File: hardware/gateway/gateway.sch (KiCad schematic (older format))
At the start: 27 parts, among them J1 FTDI, J2 Conn_Coaxial, J3 Raspberry_Pi_2_3, U1 RFM69HW, U2 DS1307Z+, U3 AP130-xxY, Y1 32768

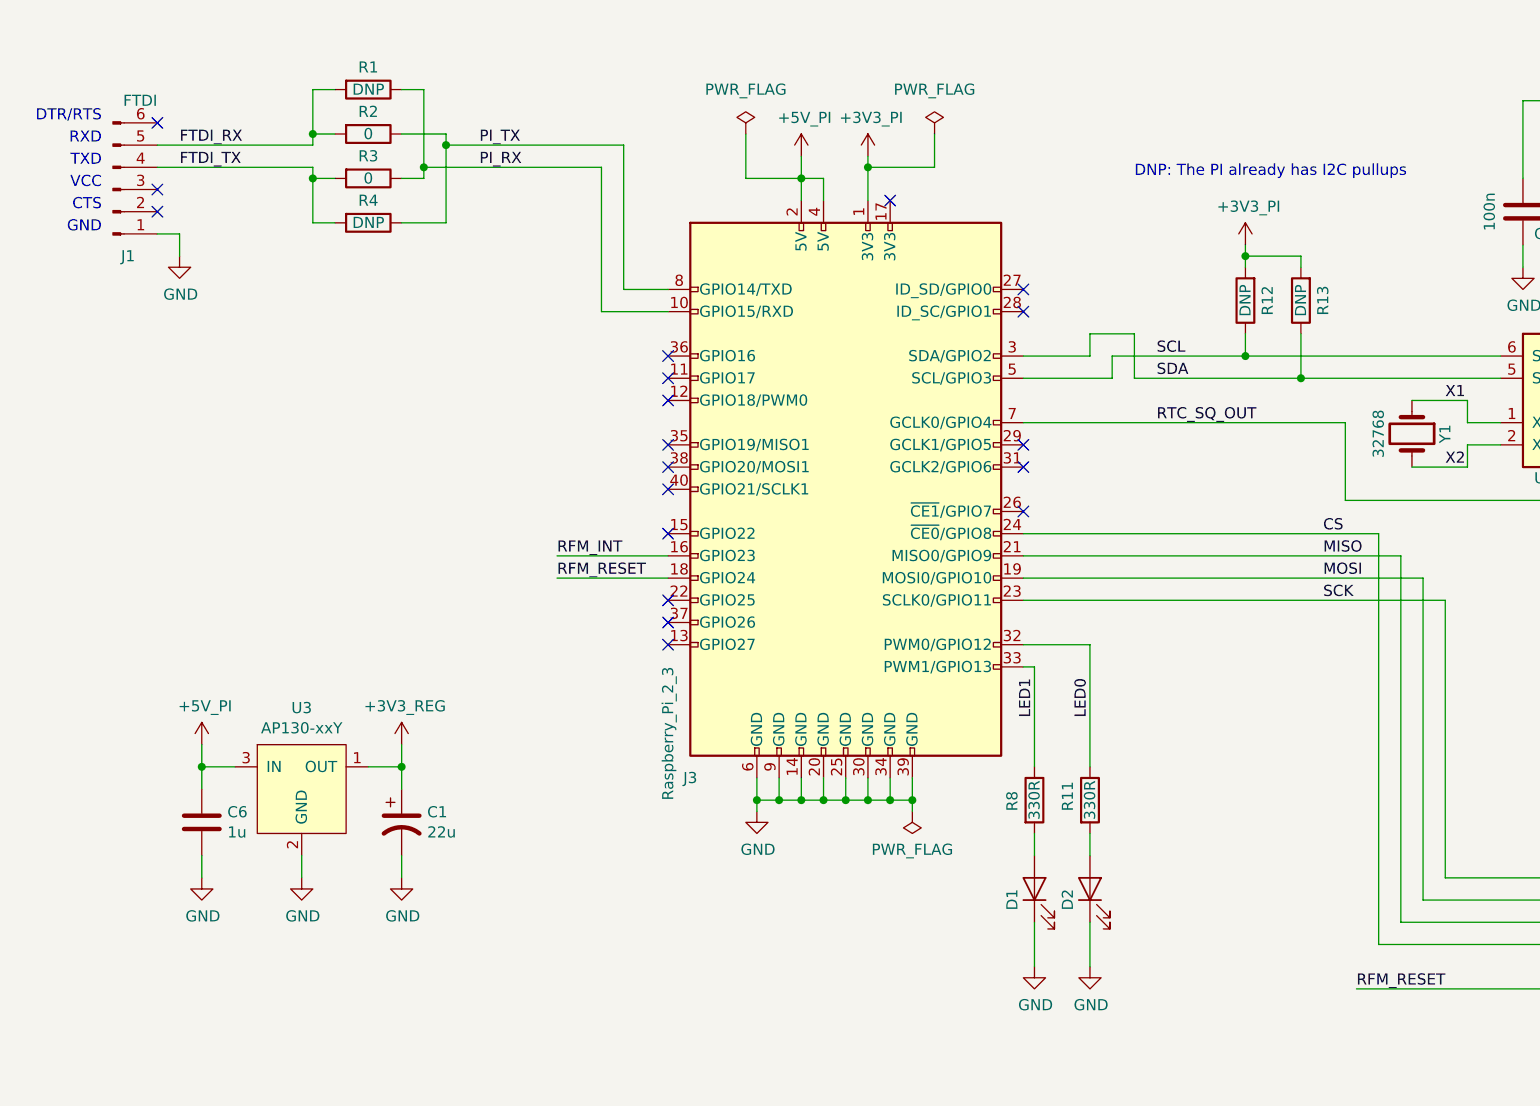
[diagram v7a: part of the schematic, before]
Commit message: Added extra input cap and CS pullup to gateway
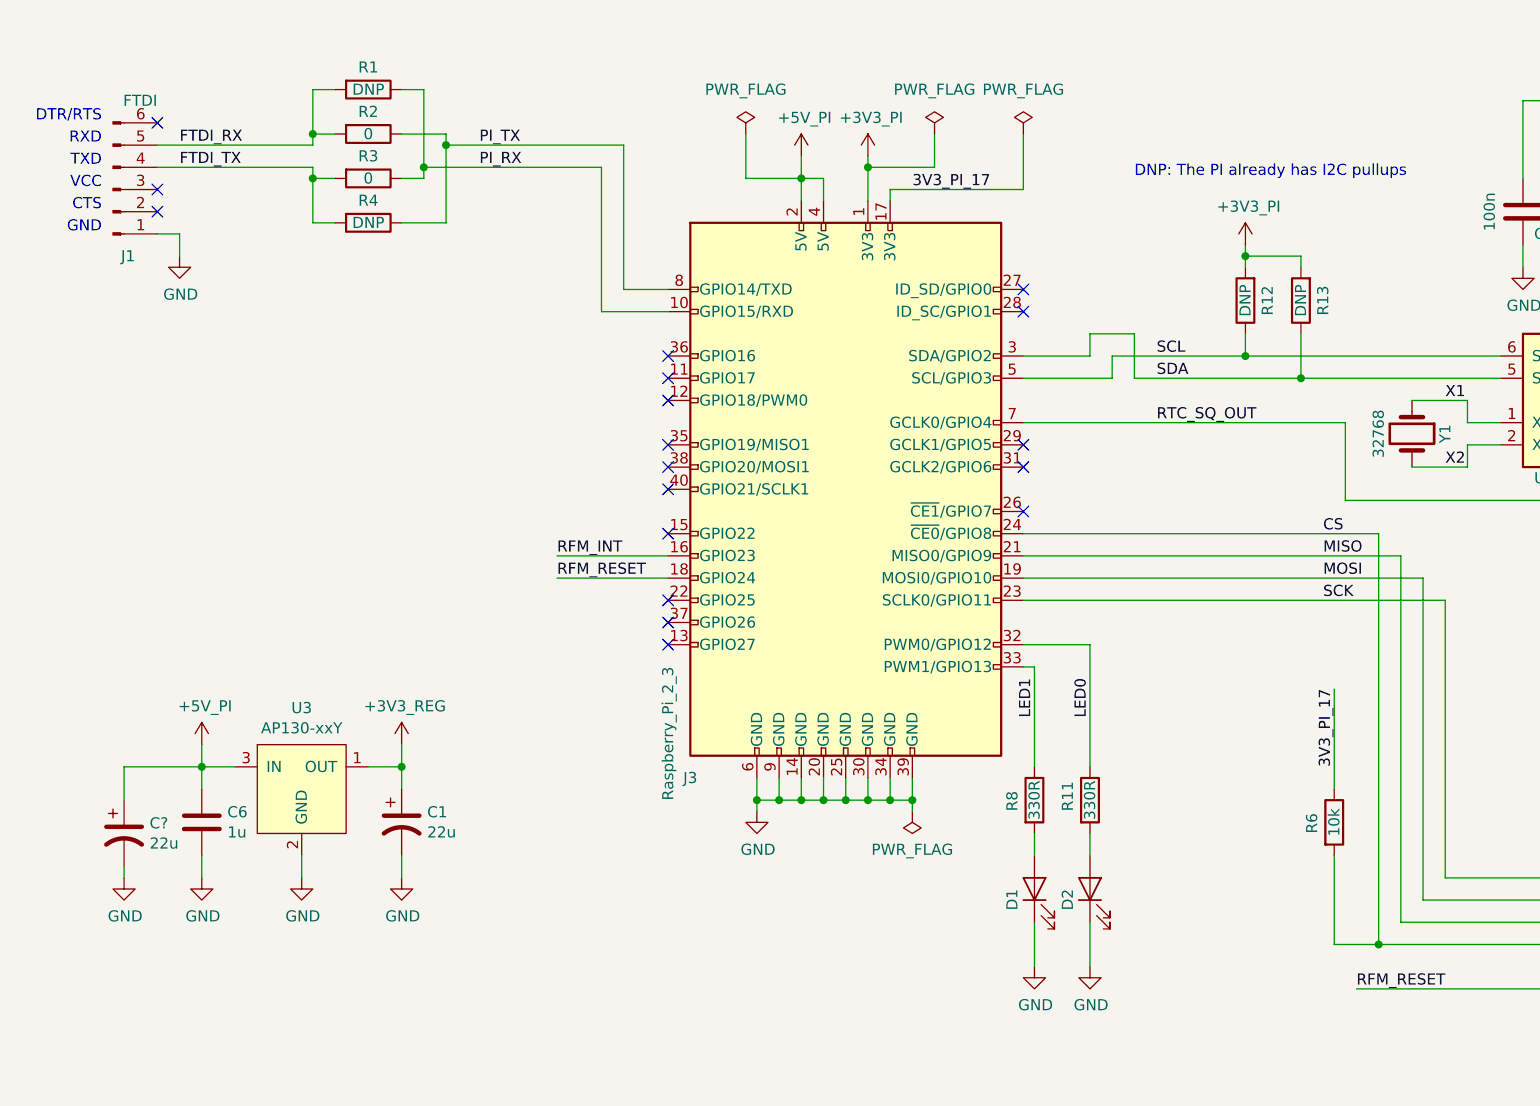
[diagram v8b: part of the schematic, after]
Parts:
- added C?: 22u, Capacitor_SMD:CP_Elec_5x5.3, symbol Device:CP1
- added R6: 10k, Resistor_SMD:R_0603_1608Metric_Pad1.05x0.95mm_HandSolder, symbol Device:R
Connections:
- net +5V_PI: now also C?.1
- net CS: now also R6.2
- net GND: now also C?.2
- net 3V3_PI_17: now reaches J3.17 (3V3)
- net 3V3_PI_17: now also R6.1
- no-connect marks 24 -> 23
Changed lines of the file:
@@
 Wire Wire Line
 	4200 1250 4200 1350
-NoConn ~ 4600 1350
 $Comp
 L humidity:+5V_PI #PWR0104
@@
 Wire Wire Line
 	3950 1250 4200 1250
+$Comp
+L Device:R R6
+U 1 1 5D2FBF60
+P 6600 4150
+F 0 "R6" V 6500 4100 50  0000 L CNN
+F 1 "10k" V 6600 4150 50  0000 C CNN
+F 2 "Resistor_SMD:R_0603_1608Metric_Pad1.05x0.95mm_HandSolder" V 6530 4150 50  0001 C CNN
+F 3 "~" H 6600 4150 50  0001 C CNN
+F 4 "https://www.tme.eu/se/en/details/crcw060310k0fktabc/0603-smd-resistors/vishay/" H -350 2350 50  0001 C CNN "TME Link"
+F 5 "0.12458" H -350 2350 50  0001 C CNN "TME Price"
+	1    6600 4150
+	1    0    0    -1
+$EndComp
+Wire Wire Line
+	6600 4300 6600 4700
+Wire Wire Line
+	6600 4700 6800 4700
+Connection ~ 6800 4700
+Wire Wire Line
+	6600 3550 6600 4000
+Wire Wire Line
+	4600 1350 4600 1300
+$Comp
+L power:PWR_FLAG #FLG0103
+U 1 1 5D30D5AE
+P 5200 1050
+F 0 "#FLG0103" H 5200 1125 50  0001 C CNN
+F 1 "PWR_FLAG" H 5200 1250 50  0000 C CNN
+F 2 "" H 5200 1050 50  0001 C CNN
+F 3 "~" H 5200 1050 50  0001 C CNN
+	1    5200 1050
+	1    0    0    -1
+$EndComp
+Wire Wire Line
+	5200 1050 5200 1300
+Text Label 4700 1300 0    50   ~ 0
+3V3_PI_17
+Wire Wire Line
+	4600 1300 5200 1300
+Text Label 6600 3900 1    50   ~ 0
+3V3_PI_17
+$Comp
+L Device:CP1 C?
+U 1 1 5D325ADD
+P 1150 4200
+F 0 "C?" H 1265 4246 50  0000 L CNN
+F 1 "22u" H 1265 4155 50  0000 L CNN
+F 2 "Capacitor_SMD:CP_Elec_5x5.3" H 1150 4200 50  0001 C CNN
+F 3 "~" H 1150 4200 50  0001 C CNN
+F 4 "https://www.tme.eu/se/en/details/sc1e226m05005vr/85degc-smd-electrolytic-capacitors/samwha/" H 1150 4200 50  0001 C CNN "TME Link"
+F 5 "0.36794" H 1150 4200 50  0001 C CNN "TME Price"
+	1    1150 4200
+	1    0    0    -1
+$EndComp
+Wire Wire Line
+	1500 3900 1150 3900
+Wire Wire Line
+	1150 3900 1150 4050
+$Comp
+L power:GND #PWR?
+U 1 1 5D32BD4F
+P 1150 4400
+F 0 "#PWR?" H 1150 4150 50  0001 C CNN
+F 1 "GND" H 1155 4227 50  0000 C CNN
+F 2 "" H 1150 4400 50  0001 C CNN
+F 3 "" H 1150 4400 50  0001 C CNN
+	1    1150 4400
+	1    0    0    -1
+$EndComp
+Wire Wire Line
+	1150 4350 1150 4400
 $EndSCHEMATC
